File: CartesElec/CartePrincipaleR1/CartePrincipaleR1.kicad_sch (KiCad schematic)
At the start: 8 parts

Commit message: update maybe?
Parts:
- added J? (x6): Conn_01x04_Male, symbol Connector:Conn_01x04_Male
- added J? (x5): Conn_01x03_Male, symbol Connector:Conn_01x03_Male
- added J?: Screw_Terminal_01x02, symbol Connector:Screw_Terminal_01x02
- added R? (x2): R, symbol Device:R
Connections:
- net +12V: now also J?.2 (Pin_2), J?.2 (Pin_2)
- net +5V: now also J?.1 (Pin_1), J?.1 (Pin_1), J?.1 (Pin_1), J?.1 (Pin_1), J?.1 (Pin_1), J?.1 (Pin_1), J?.1 (Pin_1), J?.2 (Pin_2), J?.2 (Pin_2), J?.2 (Pin_2), J?.2 (Pin_2)
- net GND: now also J?.1 (Pin_1), J?.1 (Pin_1), J?.2 (Pin_2), J?.1 (Pin_1), J?.1 (Pin_1), J?.1 (Pin_1), J?.1 (Pin_1), J?.1 (Pin_1), J?.1 (Pin_1), J?.2 (Pin_2), J?.2 (Pin_2), J?.2 (Pin_2), J?.2 (Pin_2), J?.2 (Pin_2), J?.2 (Pin_2)
- net XBee1: now reaches J?.3 (Pin_3)
- net Xbee2: now reaches J?.4 (Pin_4)
- net DataAX12: now reaches J?.3 (Pin_3), J?.3 (Pin_3)
- net PullUpI2C: now reaches A?.17 (3V3)
- net PullUpI2C: now also R?.2, R?.2
- new net MC1A: J?.3 (Pin_3)
- new net MC1B: J?.4 (Pin_4)
- new net MC2A: J?.3 (Pin_3)
- new net MC2B: J?.4 (Pin_4)
- new net Mot1DIR: J?.3 (Pin_3)
- new net Mot1PWM: J?.2 (Pin_2)
- new net Mot2DIR: J?.3 (Pin_3)
- new net Mot2PWM: J?.2 (Pin_2)
- new net RC_1A: J?.3 (Pin_3)
- new net RC_1B: J?.4 (Pin_4)
- new net RC_2A: J?.3 (Pin_3)
- new net RC_2B: J?.4 (Pin_4)
- new net S1: J?.3 (Pin_3)
- new net S2: J?.3 (Pin_3)
- new net S3: J?.3 (Pin_3)
- new net SCL_I2C: J?.4 (Pin_4), J?.4 (Pin_4), R?.1
- new net SDA_I2C: J?.3 (Pin_3), J?.3 (Pin_3), R?.1
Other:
- note added: "Ctrl Moteurs"
- note added: "Enc_Moteurs"
- note added: "I2C"
- note added: "Roue_Codeuses"
- note added: "Servos"
- note added: "Sortie 5V"

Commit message: update carte nucleo F411RE
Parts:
- added R3: R, symbol Device:R
- added R4: 10k, symbol Device:R
- added SW1, SW2, SW3, SW4: SW_SPDT, symbol Switch:SW_SPDT
- added U2: NUCLEO64-F411RE, Module:ST_Morpho_Connector_144_STLink, symbol MCU_Module:NUCLEO64-F411RE
- added U3: TM1637, DIP778W43P254L2612H431Q20N, symbol TM1637:TM1637
- gave numbers to parts that had none: 22
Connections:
- net +5V: now also R3.2, SW1.1 (A), SW2.1 (A), SW3.1 (A), SW4.1 (A), U3.16 (VDD)
- net GND: now also R4.2, SW1.3 (C), SW2.3 (C), SW3.3 (C), SW4.3 (C), U3.1 (GND)
- net Mot1DIR: now also U2.57 (PC7)
- net Mot1PWM: now also U2.59 (PA9)
- net Mot2DIR: now also U2.63 (PB10)
- net Mot2PWM: now also U2.61 (PA8)
- net S1: now also U2.28 (PA0)
- net S2: now also U2.30 (PA1)
- net SCL_I2C: now also U2.38 (PC0)
- net SDA_I2C: now also U2.36 (PC1)
- new net ADC_2: U2.72 (PC4)
- new net AD_1: U2.44 (PC5)
- new net A_Resistance: R3.1, R4.1
- new net CLK_Display: U3.18 (CLK)
- new net DIO_Display: U3.17 (DIO)
- new net PullDownB1: SW3.2 (B)
- new net PullDownB2: SW4.2 (B)
- new net PullDownC1: SW1.2 (B)
- new net PullDownC2: SW2.2 (B)
- new net USART_RX: U2.75 (STLINK_UART_RX/PA3)
- new net USART_TX: U2.73 (STLINK_UART_TX/PA2)
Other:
- note added: "I2C Capteur couleur"
- note removed: "I2C"
- moved on the sheet: A1

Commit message: update hierarchical
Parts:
- removed A1: Arduino_Nano_v3.x, Module:Arduino_Nano, symbol MCU_Module:Arduino_Nano_v3.x
- removed J11, J14, J6, J8: Conn_01x03_Male, symbol Connector:Conn_01x03_Male
- removed J12, J13, J15, J16: Conn_01x04_Male, symbol Connector:Conn_01x04_Male
- removed R3: R, symbol Device:R
- removed SW1, SW2: SW_SPDT, symbol Switch:SW_SPDT
- removed U3: TM1637, DIP778W43P254L2612H431Q20N, symbol TM1637:TM1637
- added J?: Conn_01x02_Male, symbol Connector:Conn_01x02_Male
- added J?: Conn_01x04_Male, symbol Connector:Conn_01x04_Male
- added J?: Conn_02x08_Top_Bottom, symbol Connector_Generic:Conn_02x08_Top_Bottom
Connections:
- net +5V: now also J?.1 (Pin_1), J?.1 (Pin_1)
- net A_Resistance: now also J?.2 (Pin_2)
- net CLK_Display: now also J?.4 (Pin_4)
- net DIO_Display: now also J?.3 (Pin_3)
- net GND: now also J?.2 (Pin_2)
- no-connect marks 3 -> 0
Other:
- added sheet Carte Secondaire (CarteSecondaire.kicad_sch)
- note removed: "AX12"
- note removed: "Ctrl Moteurs"
- note removed: "Enc_Moteurs"
- note removed: "Roue_Codeuses"
- moved on the sheet: J3, J7, J9

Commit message: small updates
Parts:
- removed SW3, SW4: SW_SPDT, symbol Switch:SW_SPDT
- added CONN_COL1, CONN_TIR1: Conn_01x02_Male, Connector_JST:JST_XH_B2B-XH-A_1x02_P2.50mm_Vertical, symbol Connector:Conn_01x02_Male
- added J13, J8: Conn_01x04_Male, symbol Connector:Conn_01x04_Male
- gave numbers to parts that had none: 3
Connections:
- net +5V: now also J13.4 (Pin_4), J8.4 (Pin_4)
- net GND: now also CONN_COL1.2 (Pin_2), CONN_TIR1.2 (Pin_2), J13.3 (Pin_3), J8.3 (Pin_3)
- net S3: now also U2.34 (PB0)
- net MOT_PISTON_PWM: now reaches U2.39 (PC9)
- new net CLK: J13.2 (Pin_2), J8.2 (Pin_2)
- new net COL_GPIO: CONN_COL1.1 (Pin_1)
- new net DATA_PRESS_1: J8.1 (Pin_1)
- new net DATA_PRESS_2: J13.1 (Pin_1)
- new net TIR_GPIO: CONN_TIR1.1 (Pin_1)

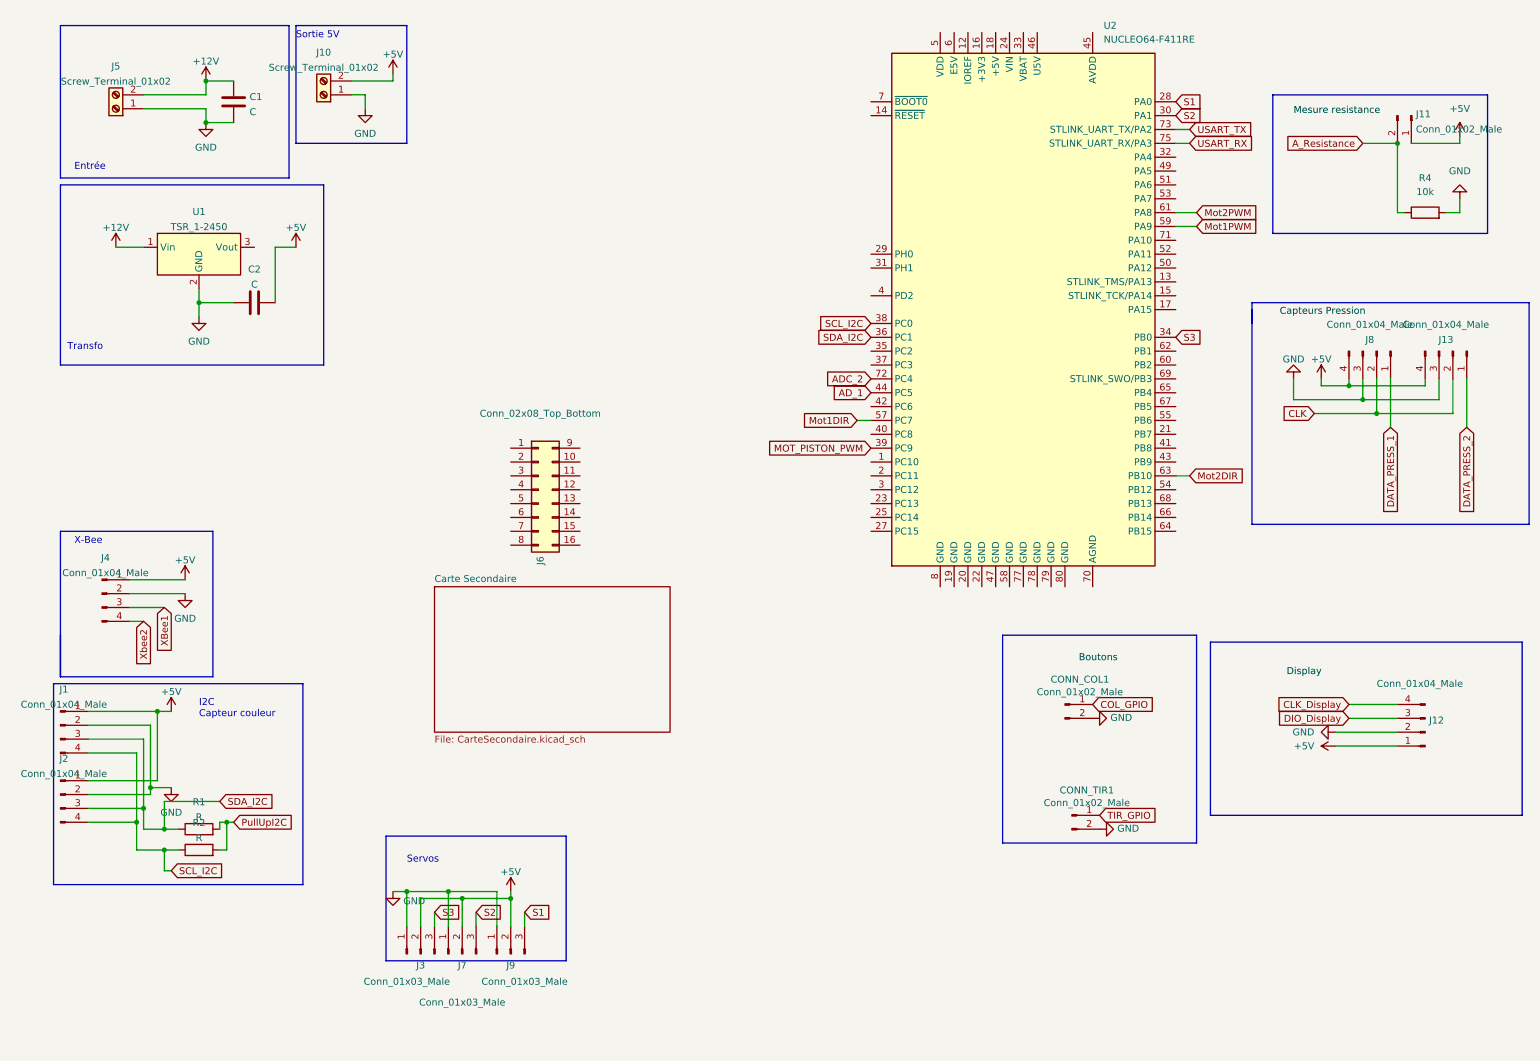
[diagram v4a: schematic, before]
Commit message: [carte robot 1] finish schematic.
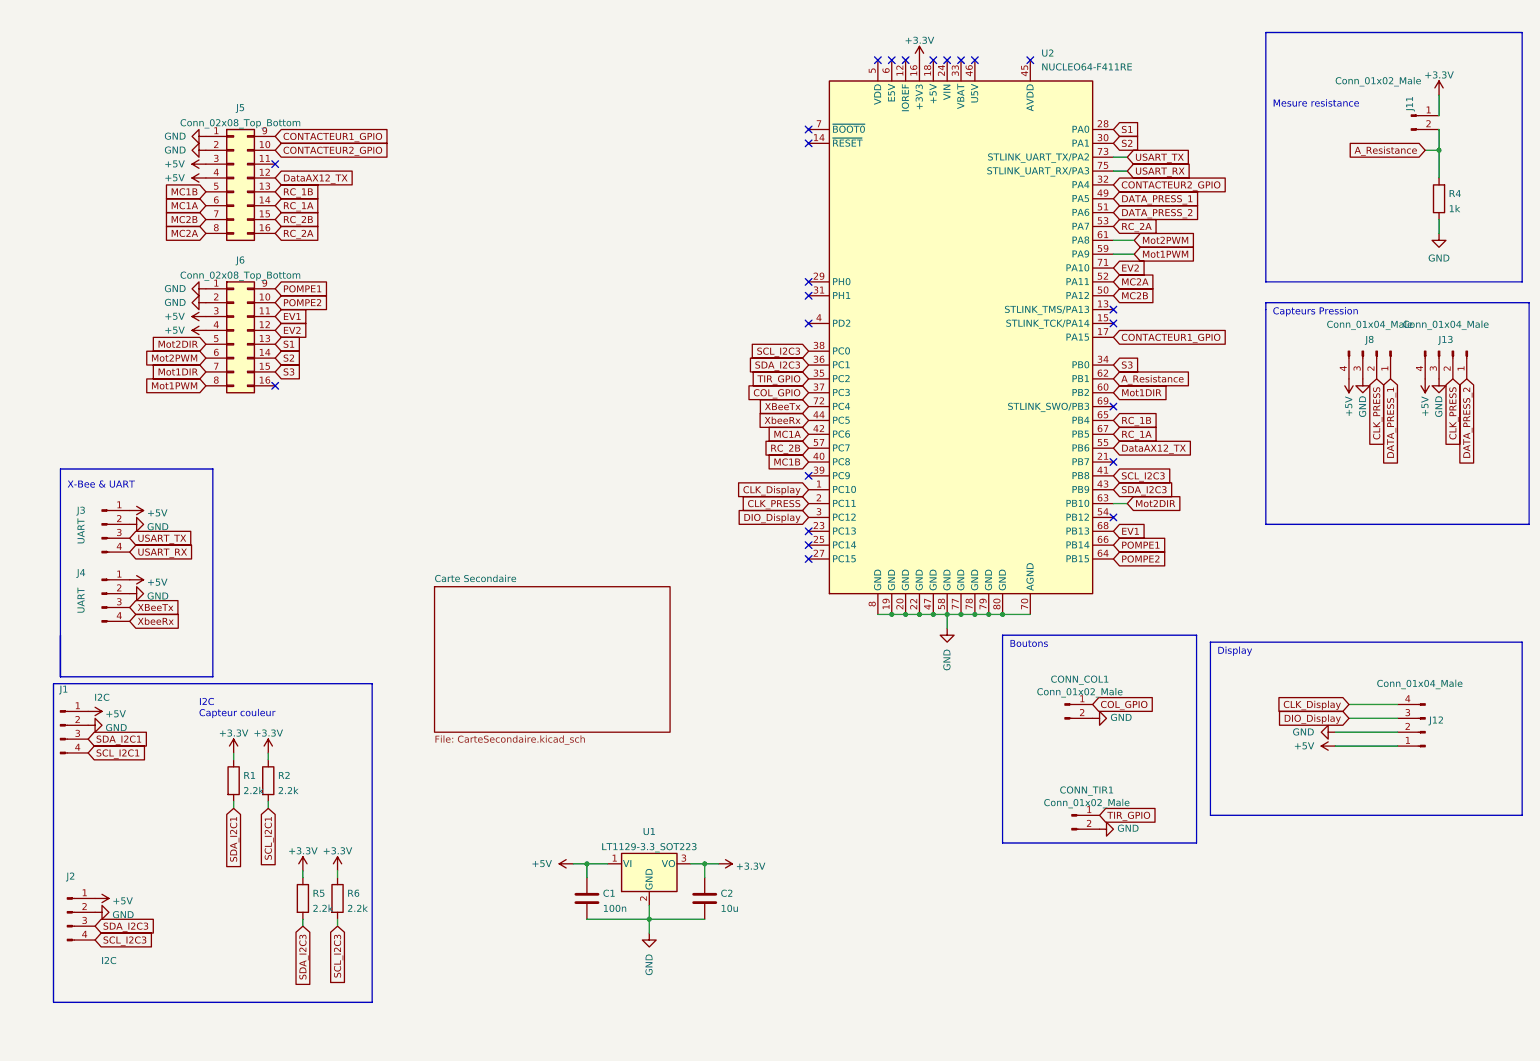
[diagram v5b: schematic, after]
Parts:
- removed J10, J5: Screw_Terminal_01x02, symbol Connector:Screw_Terminal_01x02
- removed J3, J7, J9: Conn_01x03_Male, symbol Connector:Conn_01x03_Male
- removed U1: TSR_1-2450, Converter_DCDC:Converter_DCDC_TRACO_TSR-1_THT, symbol Regulator_Switching:TSR_1-2450
- added J3: UART, symbol Connector:Conn_01x04_Male
- added J5: Conn_02x08_Top_Bottom, symbol Connector_Generic:Conn_02x08_Top_Bottom
- added R5, R6: 2.2k, symbol Device:R
- added U1: LT1129-3.3_SOT223, Package_TO_SOT_SMD:SOT-223-3_TabPin2, symbol Regulator_Linear:LT1129-3.3_SOT223
- C1: value C -> 100n
- C2: value C -> 10u
- J1, J2: value Conn_01x04_Male -> I2C
- J4: value Conn_01x04_Male -> UART
- R1, R2: value R -> 2.2k
- R4: value 10k -> 1k
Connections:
- net +12V is gone; now on net +5V: C1.1
- net CLK is gone; now on net CLK_PRESS: J13.2 (Pin_2), J8.2 (Pin_2)
- net XBee1 is gone; now on net XBeeTx: J4.3 (Pin_3)
- net Xbee2 is gone; now on net XbeeRx: J4.4 (Pin_4)
- net +5V: now also J6.3 (Pin_3), J6.4 (Pin_4), J3.1 (Pin_1), J5.3 (Pin_3), J5.4 (Pin_4), U1.1 (VI); no longer C2.2, J11.1 (Pin_1)
- net A_Resistance: now also R4.2, U2.62 (PB1); no longer R4.1
- net CLK_Display: now also U2.1 (PC10)
- net COL_GPIO: now also U2.37 (PC3)
- net DATA_PRESS_1: now also U2.49 (PA5)
- net DATA_PRESS_2: now also U2.51 (PA6)
- net DIO_Display: now also U2.3 (PC12)
- net GND: now also C2.2, J6.1 (Pin_1), J6.2 (Pin_2), R4.1, U2.19 (GND), U2.20 (GND), U2.22 (GND), U2.47 (GND), U2.58 (GND), U2.70 (AGND), U2.77 (GND), U2.78 (GND), U2.79 (GND), U2.8 (GND), U2.80 (GND), J3.2 (Pin_2), J5.1 (Pin_1), J5.2 (Pin_2), U1.2 (GND); no longer C2.1, R4.2
- net Mot1DIR: now also J6.7 (Pin_7), U2.60 (PB2); no longer U2.57 (PC7)
- net Mot1PWM: now also J6.8 (Pin_8)
- net Mot2DIR: now also J6.5 (Pin_5)
- net Mot2PWM: now also J6.6 (Pin_6)
- net S1: now also J6.13 (Pin_13)
- net S2: now also J6.14 (Pin_14)
- net S3: now also J6.15 (Pin_15)
- net TIR_GPIO: now also U2.35 (PC2)
- net USART_RX: now also J3.4 (Pin_4)
- net USART_TX: now also J3.3 (Pin_3)
- net POMPE2: now reaches J6.10 (Pin_10)
- net POMPE2: now also U2.64 (PB15)
- net EV1: now reaches J6.11 (Pin_11)
- net EV1: now also U2.68 (PB13)
- net EV2: now reaches J6.12 (Pin_12)
- net EV2: now also U2.71 (PA10)
- net POMPE1: now reaches J6.9 (Pin_9)
- net POMPE1: now also U2.66 (PB14)
- net +3V3: now reaches U2.16 (+3V3)
- net +3V3: now also C2.1, J11.1 (Pin_1), R1.1, R2.1, R5.1, R6.1, U1.3 (VO)
- net CONTACTEUR1_GPIO: now reaches U2.17 (PA15)
- net CONTACTEUR1_GPIO: now also J5.9 (Pin_9)
- net CLK_PRESS: now reaches U2.2 (PC11)
- net CONTACTEUR2_GPIO: now reaches U2.32 (PA4)
- net CONTACTEUR2_GPIO: now also J5.10 (Pin_10)
- net MC1B: now reaches U2.40 (PC8)
- net MC1B: now also J5.5 (Pin_5)
- net SCL_I2C3: now reaches U2.41 (PB8)
- net SCL_I2C3: now also J2.4 (Pin_4), U2.38 (PC0), R6.2
- net MC1A: now reaches U2.42 (PC6)
- net MC1A: now also J5.6 (Pin_6)
- net SDA_I2C3: now reaches U2.43 (PB9)
- net SDA_I2C3: now also J2.3 (Pin_3), U2.36 (PC1), R5.2
- net MC2B: now reaches U2.50 (PA12)
- net MC2B: now also J5.7 (Pin_7)
- net MC2A: now reaches U2.52 (PA11)
- net MC2A: now also J5.8 (Pin_8)
- net RC_2A: now reaches U2.53 (PA7)
- net RC_2A: now also J5.16 (Pin_16)
- net DataAX12_TX: now reaches U2.55 (PB6)
- net DataAX12_TX: now also J5.12 (Pin_12)
- net RC_1B: now reaches U2.65 (PB4)
- net RC_1B: now also J5.13 (Pin_13)
- net RC_1A: now reaches U2.67 (PB5)
- net RC_1A: now also J5.14 (Pin_14)
- net ADC_2 renamed XBeeTx
- net AD_1 renamed XbeeRx
- net MOT_PISTON_PWM: no longer names the net of U2.39 (PC9)
- net PullUpI2C renamed SCL_I2C1
- net SCL_I2C1: now also J1.4 (Pin_4); no longer R1.2
- removed net SCL_I2C: J1.4 (Pin_4), J2.4 (Pin_4), R2.1, U2.38 (PC0)
- removed net SDA_I2C: J1.3 (Pin_3), J2.3 (Pin_3), R1.1, U2.36 (PC1)
- new net RC_2B: J5.15 (Pin_15), U2.57 (PC7)
- new net SDA_I2C1: J1.3 (Pin_3), R1.2
- no-connect marks 0 -> 24
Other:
- note added: "Boutons"
- note added: "Capteurs Pression"
- note added: "Display"
- note added: "Mesure resistance"
- note added: "X-Bee & UART"
- note removed: "Entrée"
- note removed: "Servos"
- note removed: "Sortie 5V"
- note removed: "Transfo"
- note removed: "X-Bee"
- moved on the sheet: J11, J2, R1, R2, R4, U2

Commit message: Add HE14 footprints.
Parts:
- J3, J4: footprint (none) -> library:HE14_EMBASE_1x04
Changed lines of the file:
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@@
     (property "Reference" "J3" (id 0) (at 17.78 102.87 0))
     (property "Value" "UART" (id 1) (at 17.78 106.68 90))
-    (property "Footprint" "" (id 2) (at 21.59 105.41 0)
+    (property "Footprint" "library:HE14_EMBASE_1x04" (id 2) (at 21.59 105.41 0)
       (effects (font (size 1.27 1.27)) hide)
     )
@@
     (property "Reference" "J4" (id 0) (at 17.78 114.3 0))
     (property "Value" "UART" (id 1) (at 17.78 119.38 90))
-    (property "Footprint" "" (id 2) (at 21.59 118.11 0)
+    (property "Footprint" "library:HE14_EMBASE_1x04" (id 2) (at 21.59 118.11 0)
       (effects (font (size 1.27 1.27)) hide)
     )
@@
     )
     (path "/5cb3baf7-a6ae-4f22-9feb-d8d5fbeddf89/13c4a1df-b40d-402e-9343-5efea0ffdf4c"
-      (reference "CONN_COL2") (unit 1) (value "POMPE") (footprint "Connector_JST:JST_XH_B2B-XH-A_1x02_P2.50mm_Vertical")
+      (reference "CONN_COL2") (unit 1) (value "POMPE") (footprint "library:HE14_EMBASE_1x02")
     )
     (path "/5cb3baf7-a6ae-4f22-9feb-d8d5fbeddf89/d087d9ba-7b4f-41d0-afac-e2dbf443a17a"
@@
     )
     (path "/0f80c89c-6586-4e9e-ae2d-22d190abbe8c"
-      (reference "J3") (unit 1) (value "UART") (footprint "")
+      (reference "J3") (unit 1) (value "UART") (footprint "library:HE14_EMBASE_1x04")
     )
     (path "/7f63397a-af7f-44e1-b9e5-f72bc40825a5"
-      (reference "J4") (unit 1) (value "UART") (footprint "")
+      (reference "J4") (unit 1) (value "UART") (footprint "library:HE14_EMBASE_1x04")
     )
     (path "/551b8613-eb34-49fc-8c08-6e73d6cbde4b"
